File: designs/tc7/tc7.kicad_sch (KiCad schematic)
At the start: 19 parts, among them J1001 SSM-104-L-SV, P1 TC2030, U1001 MCP6001-OT

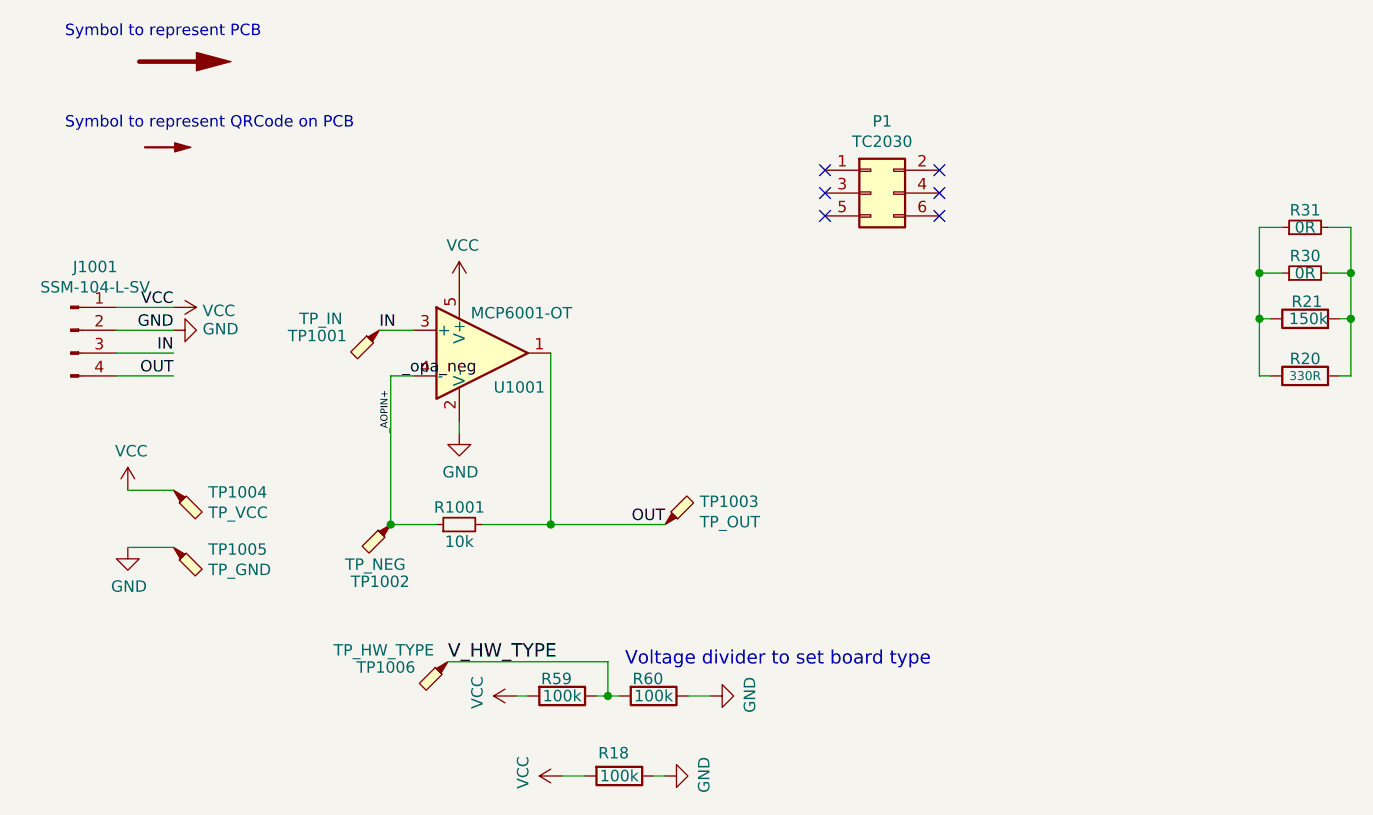
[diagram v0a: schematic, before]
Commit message: Tag KiCAD 6 version in tc7 directory for diffing
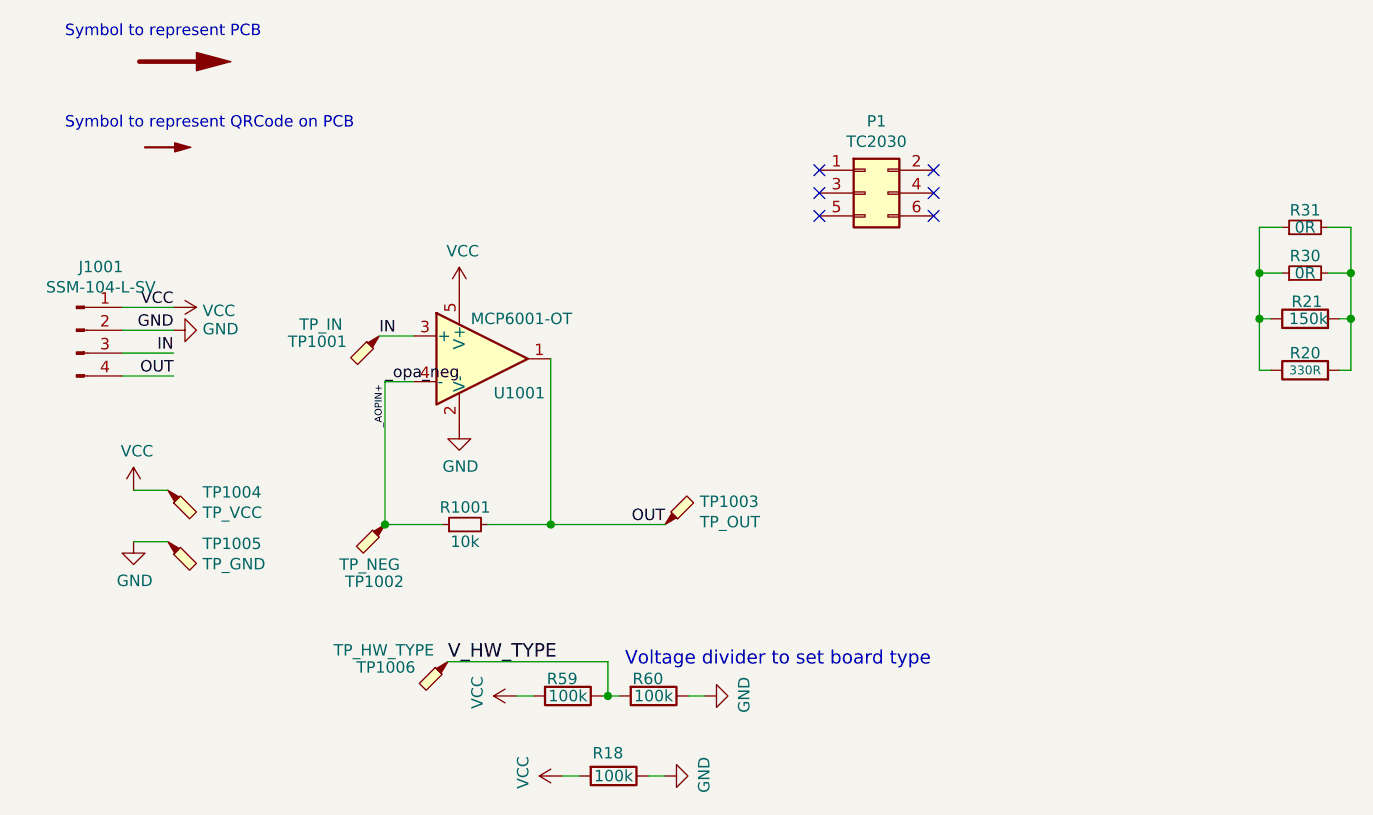
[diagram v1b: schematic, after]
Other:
- moved on the sheet: J1001, P1, R1001, R18, R20, R59, TP1001, TP1002, TP1004, TP1005, U1001

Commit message: Back to kicad7
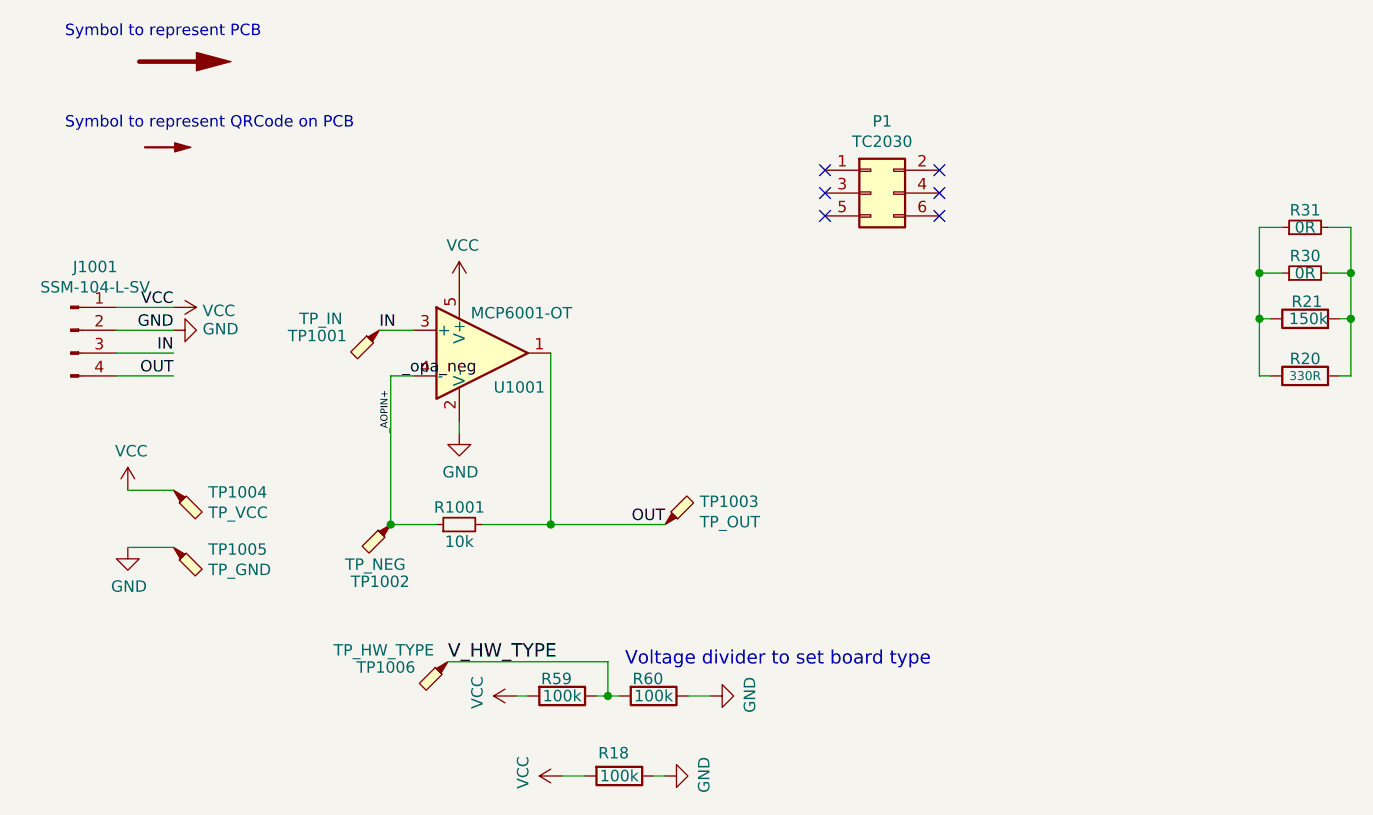
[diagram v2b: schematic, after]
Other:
- moved on the sheet: J1001, P1, R1001, R18, R20, R59, TP1001, TP1002, TP1004, TP1005, U1001
